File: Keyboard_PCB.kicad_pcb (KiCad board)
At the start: 2 copper layers, 50 x 50 mm, 24 parts, among them CON1 PS/2_JACK, CON2 USB_JACK, IC1 FT232RL, U1 ATMEGA328, X1 CRYSTAL

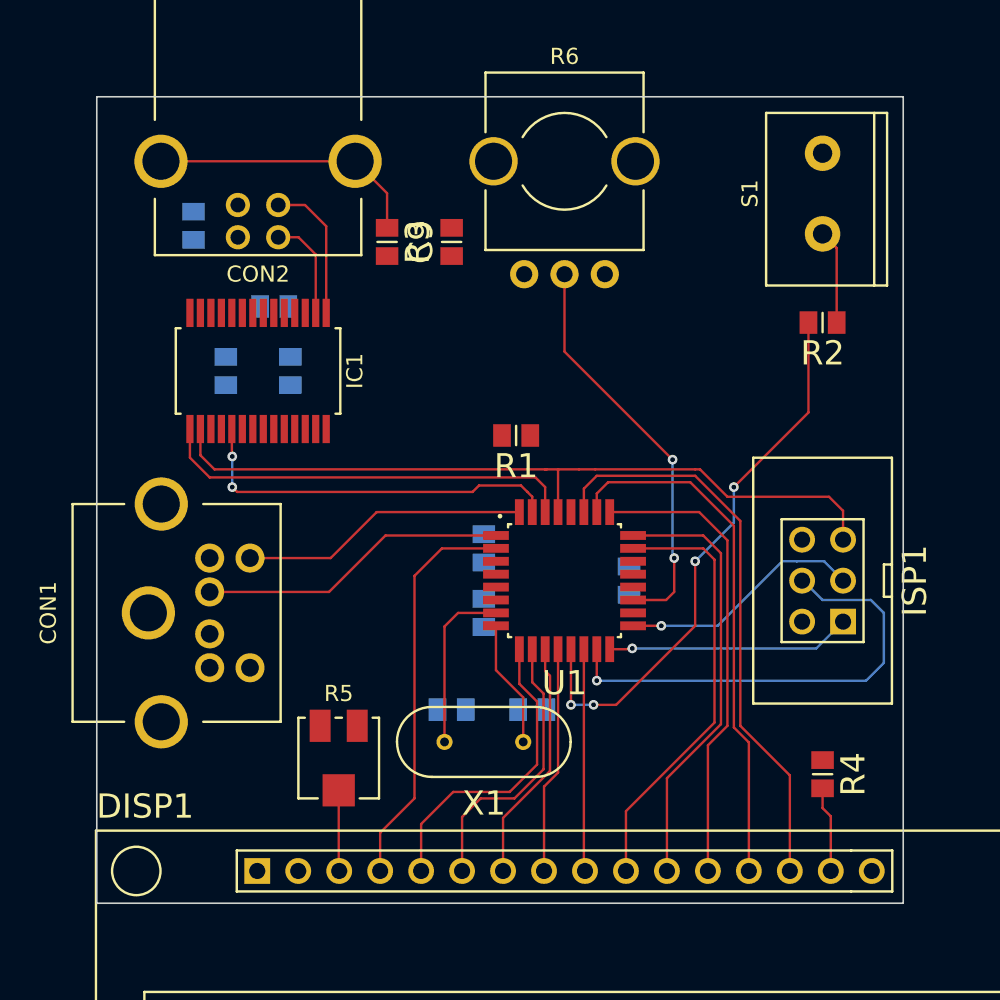
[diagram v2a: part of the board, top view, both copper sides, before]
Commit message: Added power routes and made it pass DRC.
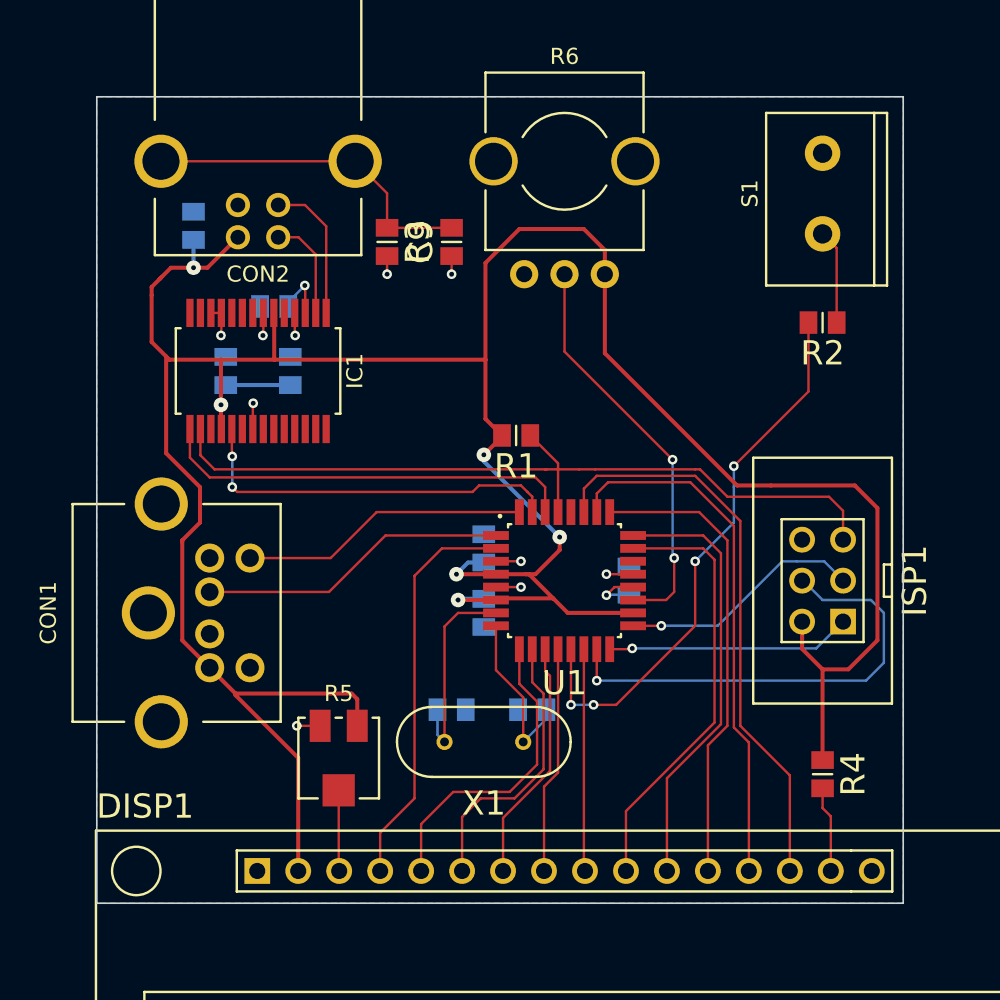
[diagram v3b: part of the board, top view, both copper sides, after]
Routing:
- net +5V: track 0.00 -> 193.6 mm, vias 0 -> 6
- net GND: track 0.00 -> 14.9 mm, vias 0 -> 10
- net N-0000031: track 17.0 -> 21.0 mm
- net N-000003: track 0.00 -> 3.43 mm, vias 0 -> 1
- net N-0000020: track 0.00 -> 3.27 mm, vias 0 -> 1
- net RESET: track 47.4 -> 50.3 mm
- net N-0000039: track 7.90 -> 10.5 mm
- net N-0000038: track 10.7 -> 12.9 mm
- added copper zone on B.Cu, net GND
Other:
- net class Vcc added: clearance 0.25, trace_width 0.25, via_dia 0.9, via_drill 0.5
